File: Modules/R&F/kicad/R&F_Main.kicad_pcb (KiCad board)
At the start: 2 copper layers, 14.5 x 108.6 mm, 29 parts, among them U1 TL074, U2 TL072

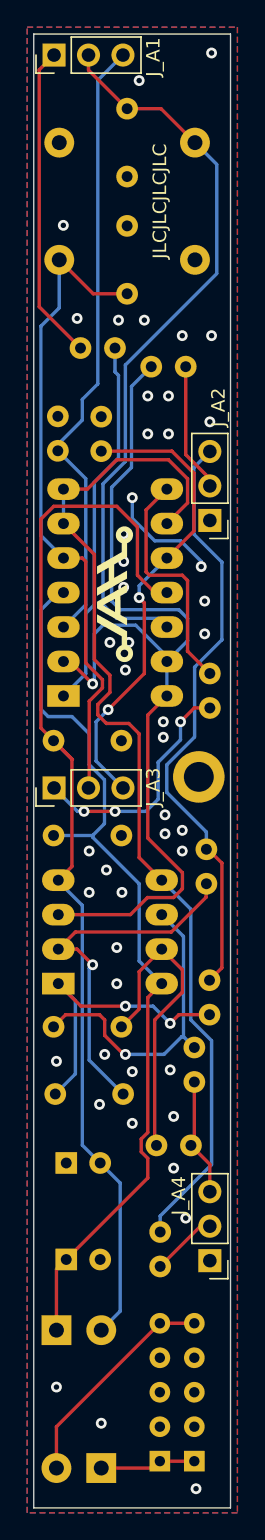
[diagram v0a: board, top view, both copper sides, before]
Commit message: Add Interactive BOMs, resave all PCBs, move VU to THT.
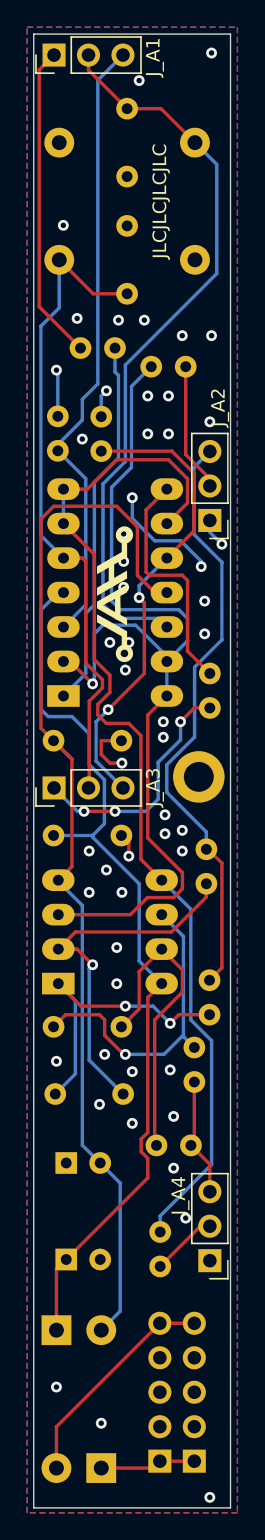
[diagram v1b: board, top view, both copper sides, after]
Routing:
- net GND: track 8.30 -> 22.0 mm, vias 47 -> 53
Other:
- board text added: "R&F v1.1"
- board text removed: "R&F v1.0"
